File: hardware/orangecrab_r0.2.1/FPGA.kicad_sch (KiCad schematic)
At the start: 14 parts, among them J6 Conn_01x05_Male, U3 LFE5U-25F-8MG285C, U6 W25Q128JVP

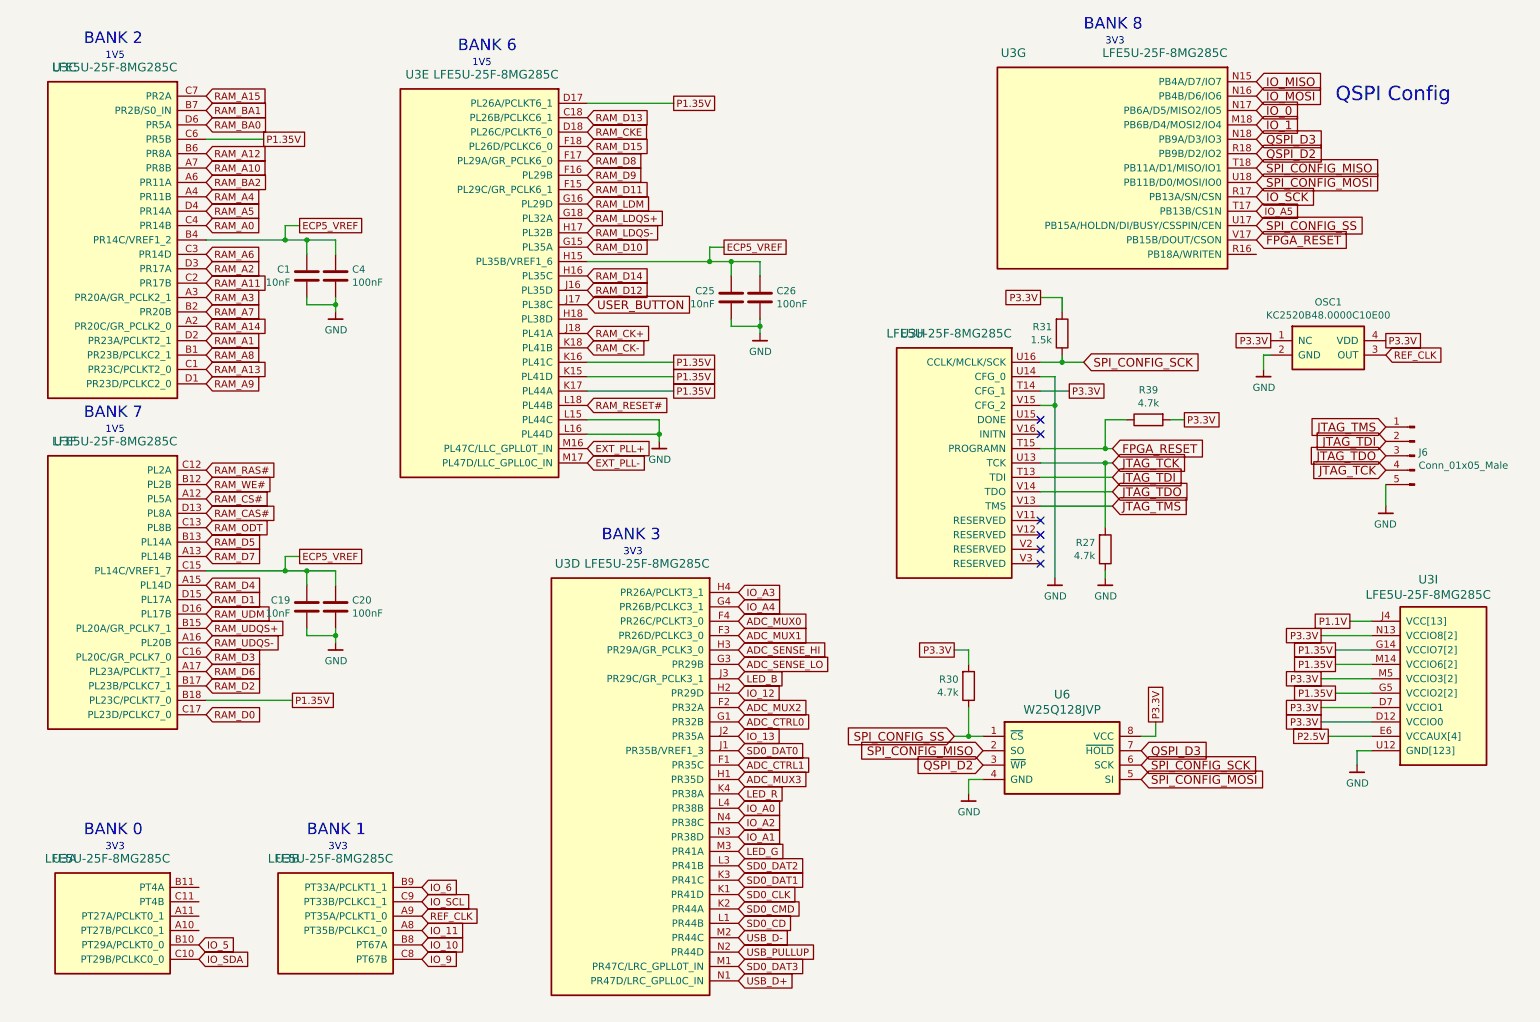
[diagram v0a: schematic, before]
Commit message: hw.r0p2p1: Copy/Paste FPGA sheet contents
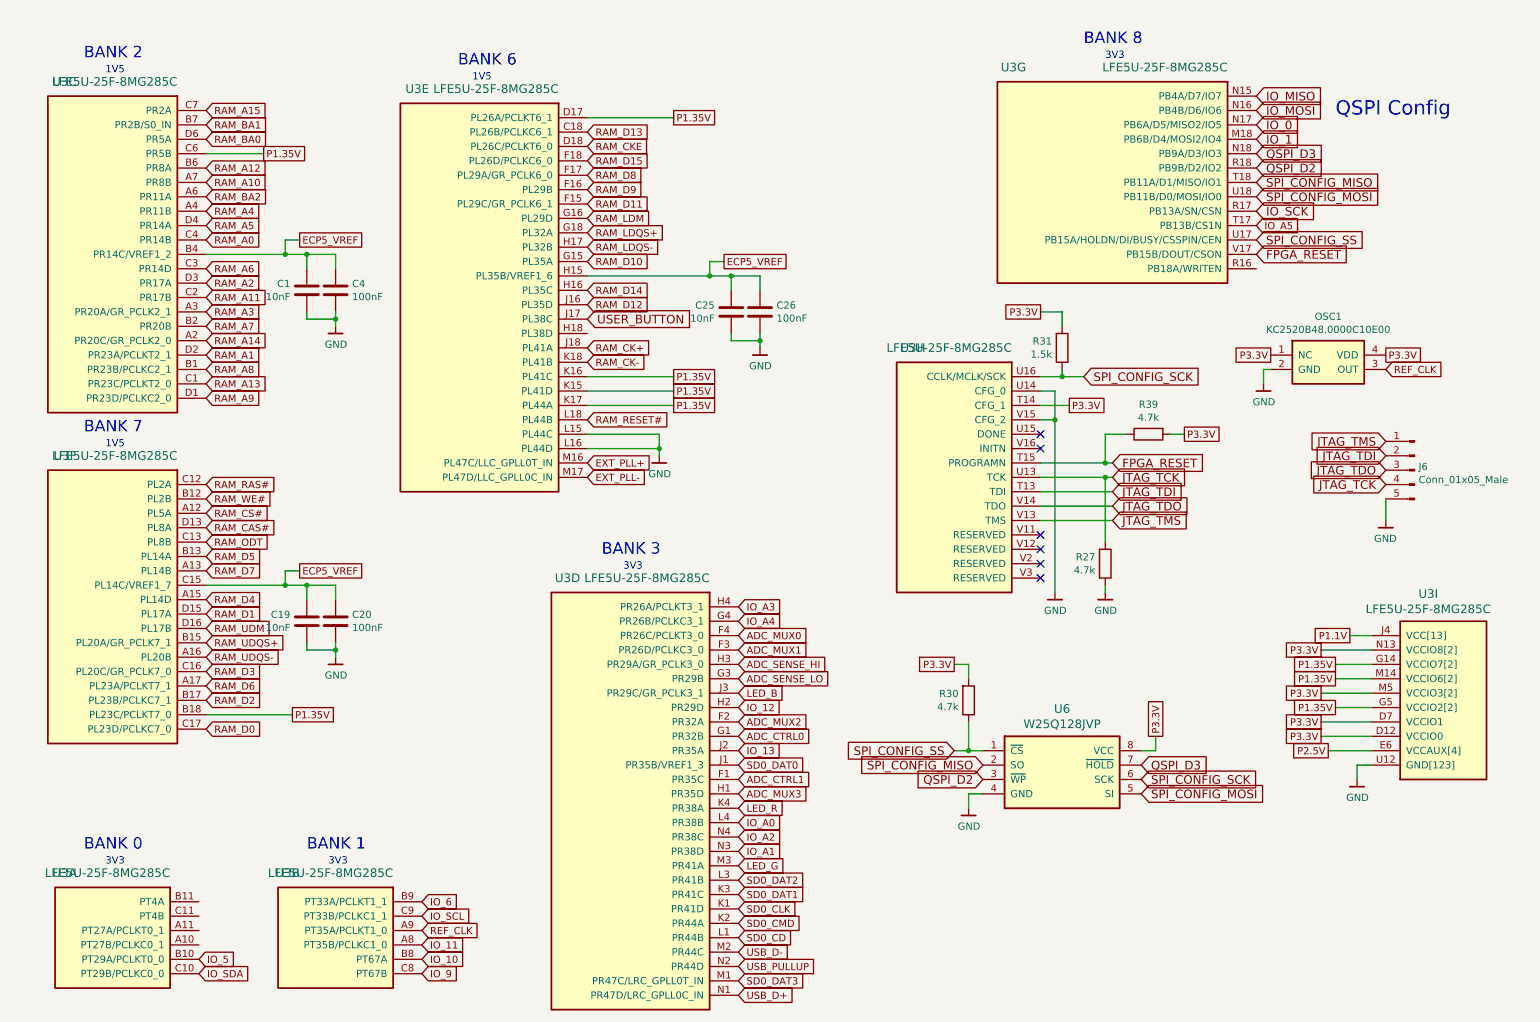
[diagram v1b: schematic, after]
